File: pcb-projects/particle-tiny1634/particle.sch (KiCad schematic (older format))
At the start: 16 parts, among them IC1 ATTINY1634-SU, P1 CONN_02X03, P2 CONN_02X03

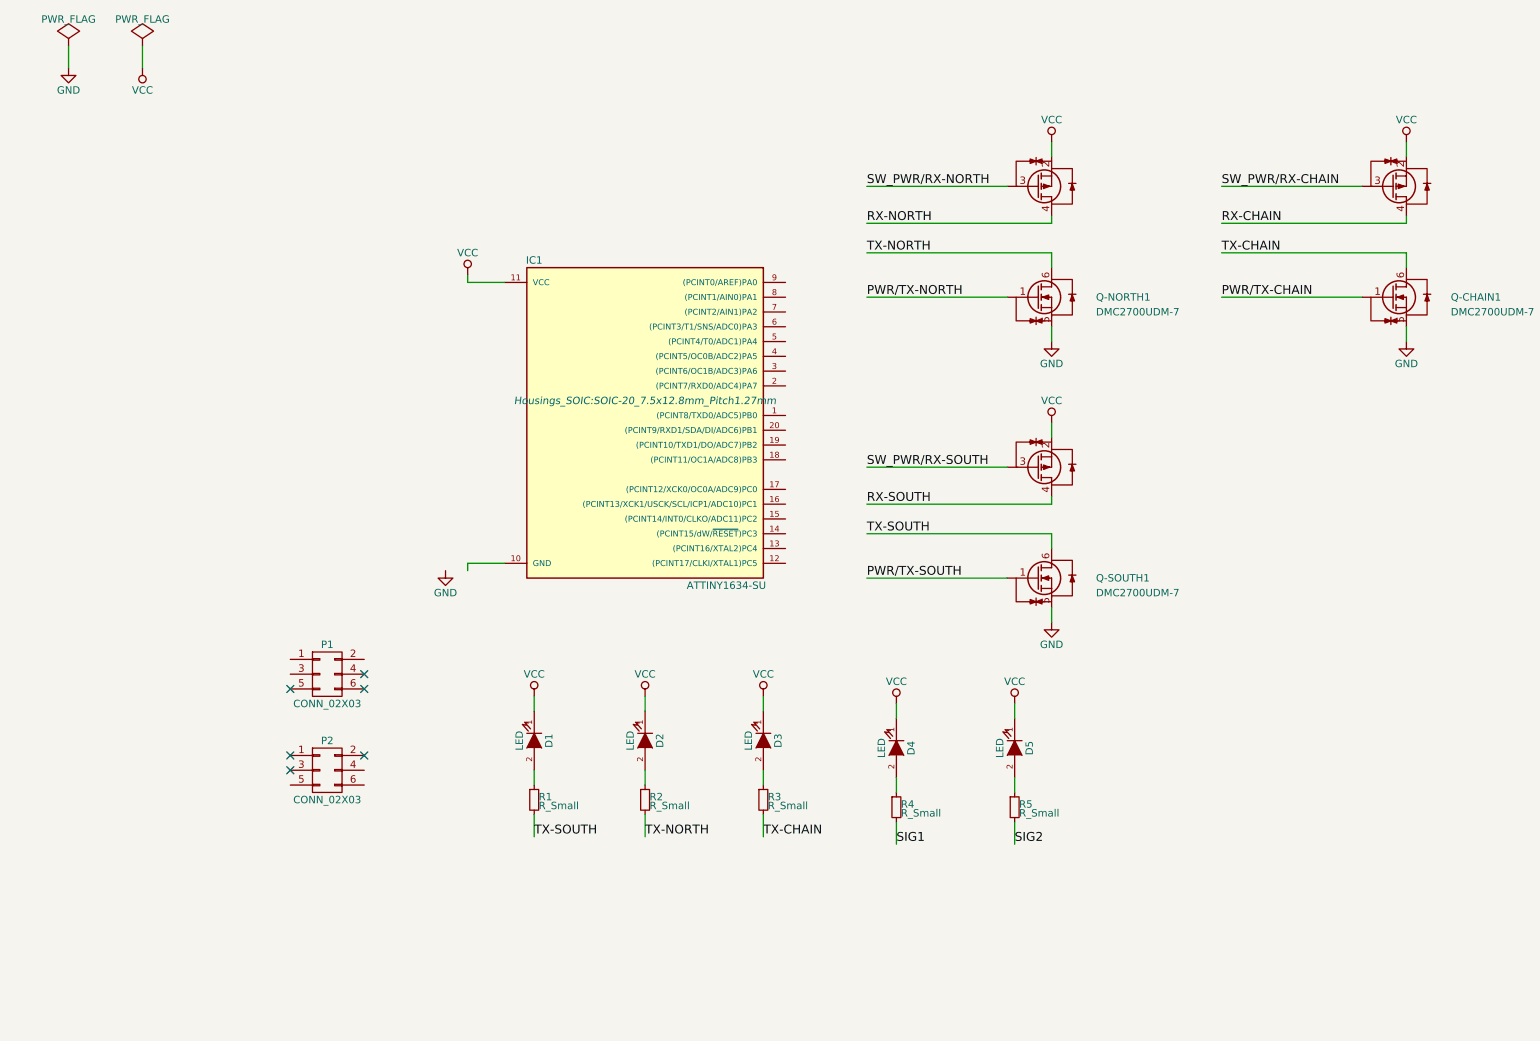
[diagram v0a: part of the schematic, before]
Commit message: routed attiny1634 particle
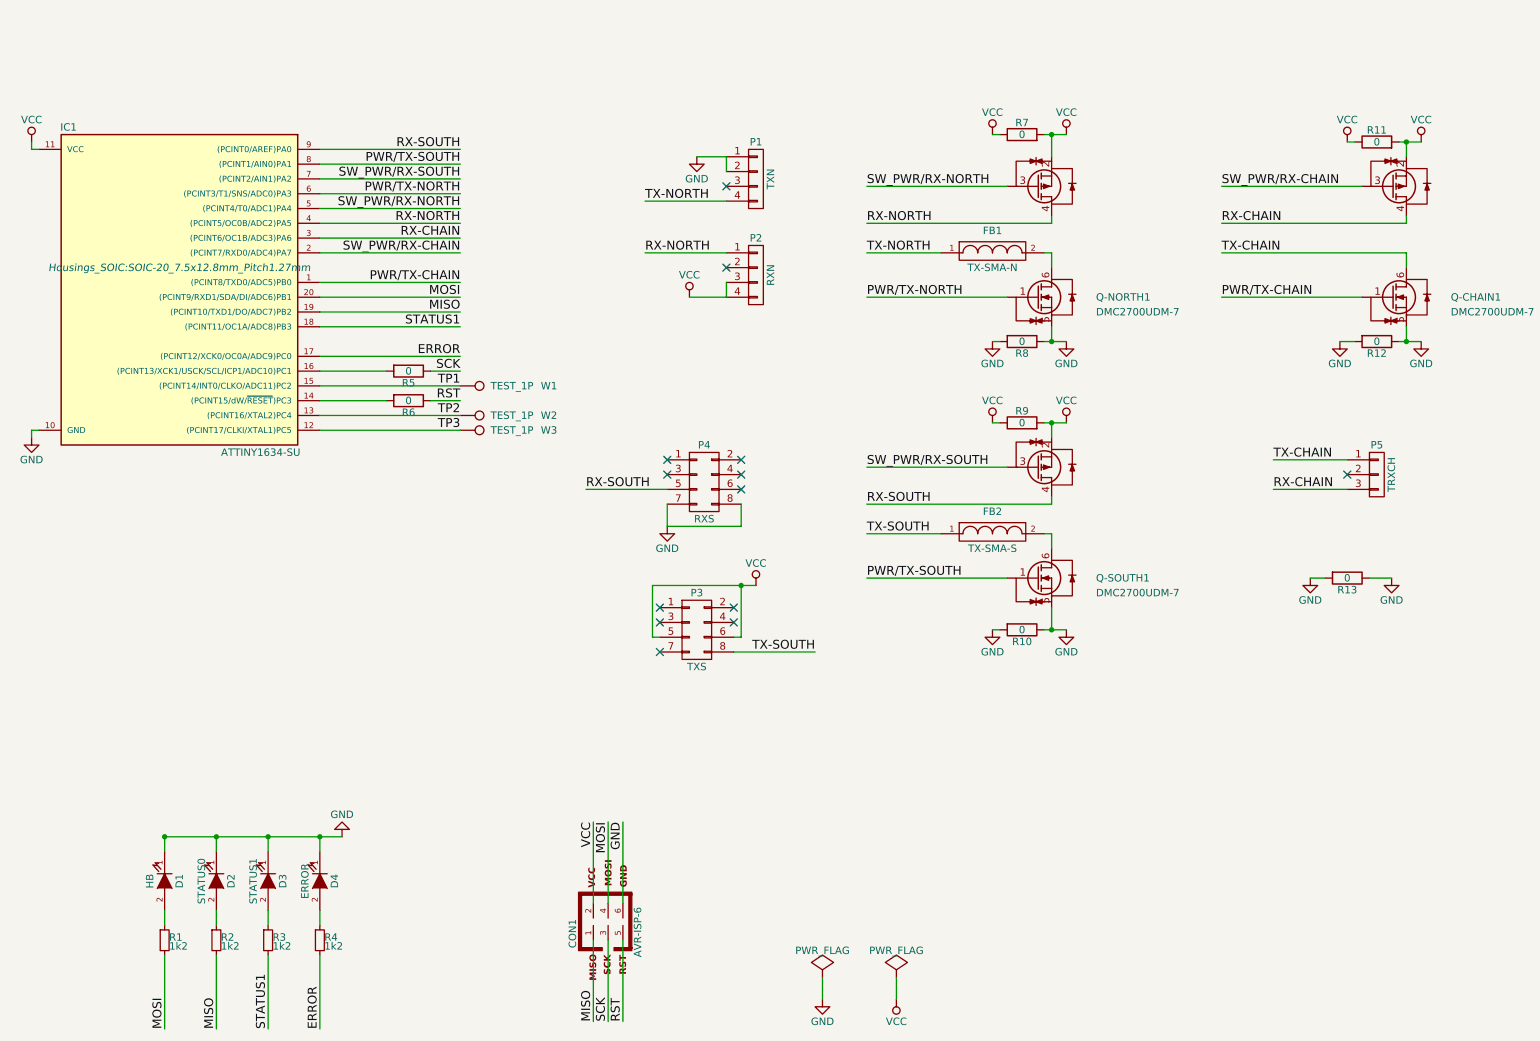
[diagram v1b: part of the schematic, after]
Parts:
- removed D1, D2: LED, LEDs:LED-1206, symbol LED
- removed P1: CONN_02X03, SMT_PIN_HEADER:CONN-6_1-3, symbol CONN_02X03
- removed P2: CONN_02X03, SMT_PIN_HEADER:CONN-6_4-6, symbol CONN_02X03
- removed R1, R2: R_Small, SMD_Packages:SMD-1206_Pol, symbol R_Small
- added CON1: AVR-ISP-6, SMT_PIN_HEADER:CONN-6, symbol AVR-ISP-6
- added D4: ERROR, Resistors_SMD:R_1206_HandSoldering, symbol LED
- added FB1: TX-SMA-N, SMD_Packages:SMD-2010_Pol, symbol FILTER
- added FB2: TX-SMA-S, SMD_Packages:SMD-2010_Pol, symbol FILTER
- added P1: TXN, SMT_PIN_HEADER:CONN-8_1-4, symbol CONN_01X04
- added P2: RXN, SMT_PIN_HEADER:CONN-8_1-4, symbol CONN_01X04
- added P3: TXS, SMT_PIN_HEADER:CONN-8_5-8, symbol CONN_02X04
- added P4: RXS, SMT_PIN_HEADER:CONN-8_5-8, symbol CONN_02X04
- added P5: TRXCH, SMT_PIN_HEADER:CONN-1x3, symbol CONN_01X03
- added R10, R11, R12, R13, R5, R6, R7, R8, R9: 0, Resistors_SMD:R_1206_HandSoldering, symbol R
- added R4: 1k2, Resistors_SMD:R_1206_HandSoldering, symbol R_Small
- added W1, W2, W3: TEST_1P, Measurement_Points:Measurement_Point_Square-SMD-Pad_Big, symbol TEST_1P
- D1: renamed from D4; value LED -> HB; footprint LEDs:LED-1206 -> Resistors_SMD:R_1206_HandSoldering
- D2: renamed from D5; value LED -> STATUS0; footprint LEDs:LED-1206 -> Resistors_SMD:R_1206_HandSoldering
- D3: value LED -> STATUS1; footprint LEDs:LED-1206 -> Resistors_SMD:R_1206_HandSoldering
- R1: renamed from R4; value R_Small -> 1k2; footprint SMD_Packages:SMD-1206_Pol -> Resistors_SMD:R_1206_HandSoldering
- R2: renamed from R5; value R_Small -> 1k2; footprint SMD_Packages:SMD-1206_Pol -> Resistors_SMD:R_1206_HandSoldering
- R3: value R_Small -> 1k2; footprint SMD_Packages:SMD-1206_Pol -> Resistors_SMD:R_1206_HandSoldering
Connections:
- net SIG1 is gone; now on net MOSI: R1.2
- net SIG2 is gone; now on net MISO: R2.2
- net GND: now also D1.1 (K), D2.1 (K), D3.1 (K), IC1.10 (GND), CON1.6, D4.1 (K), P1.1 (P1), P1.2 (P2), P4.7 (P7), P4.8 (P8), R10.1, R10.2, R12.1, R12.2, R13.1, R13.2, R8.1, R8.2
- net PWR/TX-CHAIN: now also IC1.1 ((PCINT8/TXD0/ADC5)PB0)
- net PWR/TX-NORTH: now also IC1.6 ((PCINT3/T1/SNS/ADC0)PA3)
- net PWR/TX-SOUTH: now also IC1.8 ((PCINT1/AIN0)PA1)
- net RX-CHAIN: now also IC1.3 ((PCINT6/OC1B/ADC3)PA6), P5.3 (P3)
- net RX-NORTH: now also IC1.4 ((PCINT5/OC0B/ADC2)PA5), P2.1 (P1)
- net RX-SOUTH: now also IC1.9 ((PCINT0/AREF)PA0), P4.5 (P5)
- net SW_PWR/RX-CHAIN: now also IC1.2 ((PCINT7/RXD0/ADC4)PA7)
- net SW_PWR/RX-NORTH: now also IC1.5 ((PCINT4/T0/ADC1)PA4)
- net SW_PWR/RX-SOUTH: now also IC1.7 ((PCINT2/AIN1)PA2)
- net TX-CHAIN: now also P5.1 (P1); no longer R3.2
- net TX-NORTH: now also FB1.1, P1.4 (P4); no longer Q-NORTH1.6 (D1)
- net TX-SOUTH: now also FB2.1, P3.8 (P8); no longer Q-SOUTH1.6 (D1)
- net VCC: now also CON1.2, P2.3 (P3), P2.4 (P4), P3.5 (P5), P3.6 (P6), R11.1, R11.2, R7.1, R7.2, R9.1, R9.2; no longer D1.1 (K), D2.1 (K), D3.1 (K)
- net TP3: now reaches IC1.12 ((PCINT17/CLKI/XTAL1)PC5)
- net TP3: now also W3.1
- net TP2: now reaches IC1.13 ((PCINT16/XTAL2)PC4)
- net TP2: now also W2.1
- net at IC1.14 ((PCINT15/dW/~RESET~)PC3): now also R6.2
- net TP1: now reaches IC1.15 ((PCINT14/INT0/CLKO/ADC11)PC2)
- net TP1: now also W1.1
- net at IC1.16 ((PCINT13/XCK1/USCK/SCL/ICP1/ADC10)PC1): now also R5.2
- net ERROR: now reaches IC1.17 ((PCINT12/XCK0/OC0A/ADC9)PC0)
- net ERROR: now also R4.2
- net STATUS1: now reaches IC1.18 ((PCINT11/OC1A/ADC8)PB3)
- net STATUS1: now also R3.2
- net MISO: now reaches IC1.19 ((PCINT10/TXD1/DO/ADC7)PB2)
- net MISO: now also CON1.1
- net MOSI: now reaches IC1.20 ((PCINT9/RXD1/SDA/DI/ADC6)PB1)
- net MOSI: now also CON1.4
- new net: FB1.2, Q-NORTH1.6 (D1)
- new net: FB2.2, Q-SOUTH1.6 (D1)
- new net: D4.2 (A), R4.1
- new net RST: CON1.5, R6.1
- new net SCK: CON1.3, R5.1
- no-connect marks 6 -> 13
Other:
- moved on the sheet: D1, D2, IC1, R1, R2

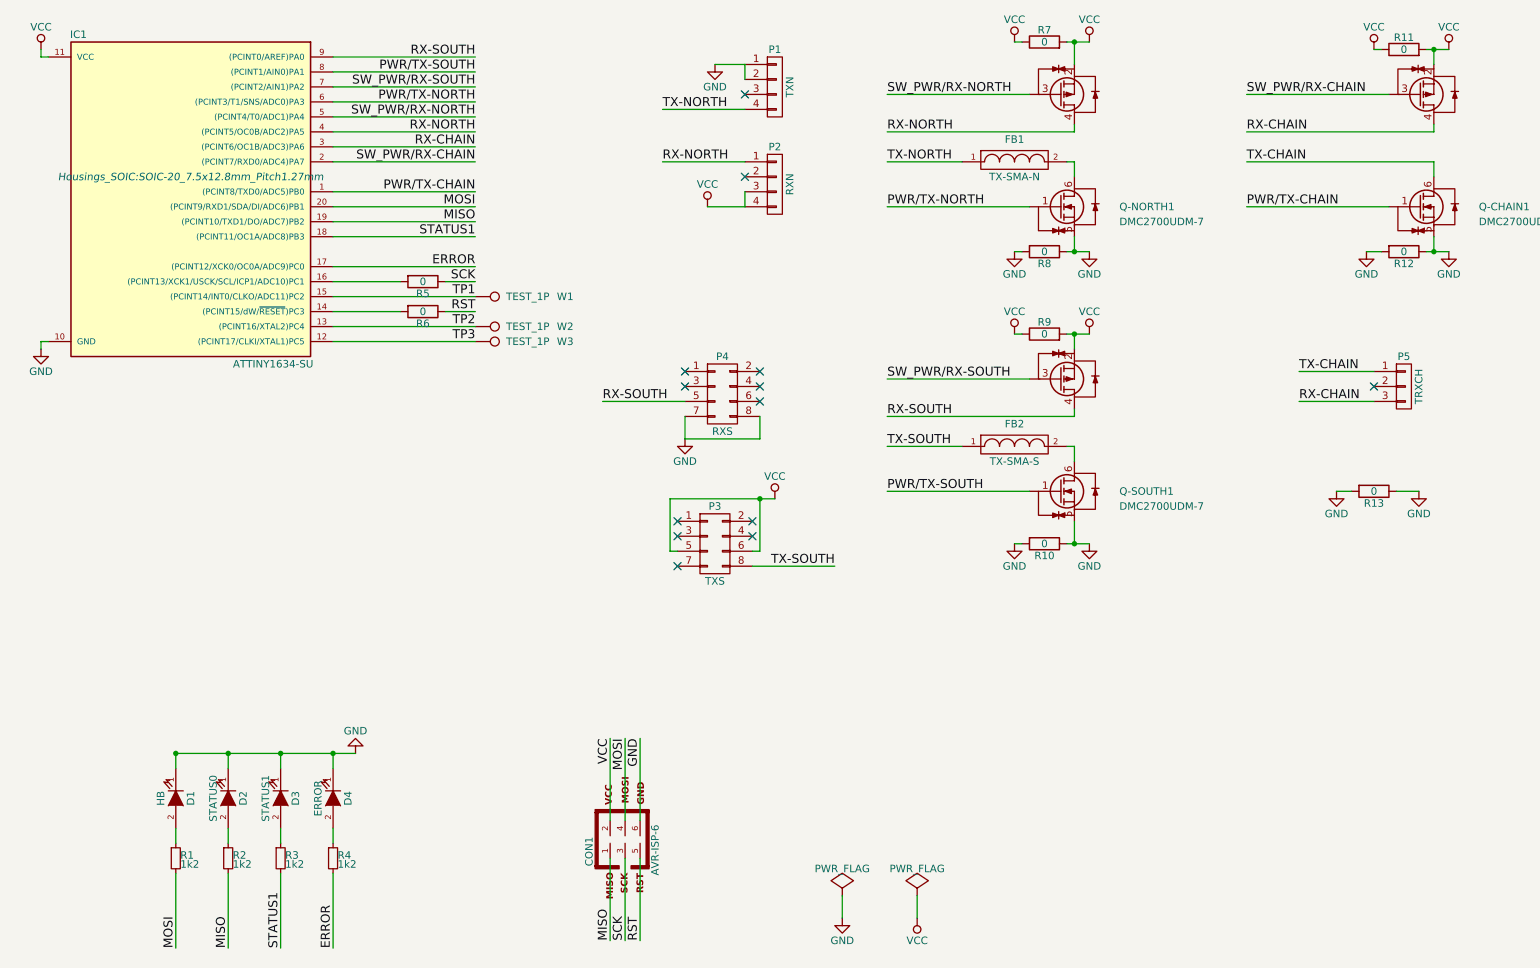
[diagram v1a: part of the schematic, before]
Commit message: re-routed smaller pcb, added several 3d packages, min. fix in schema
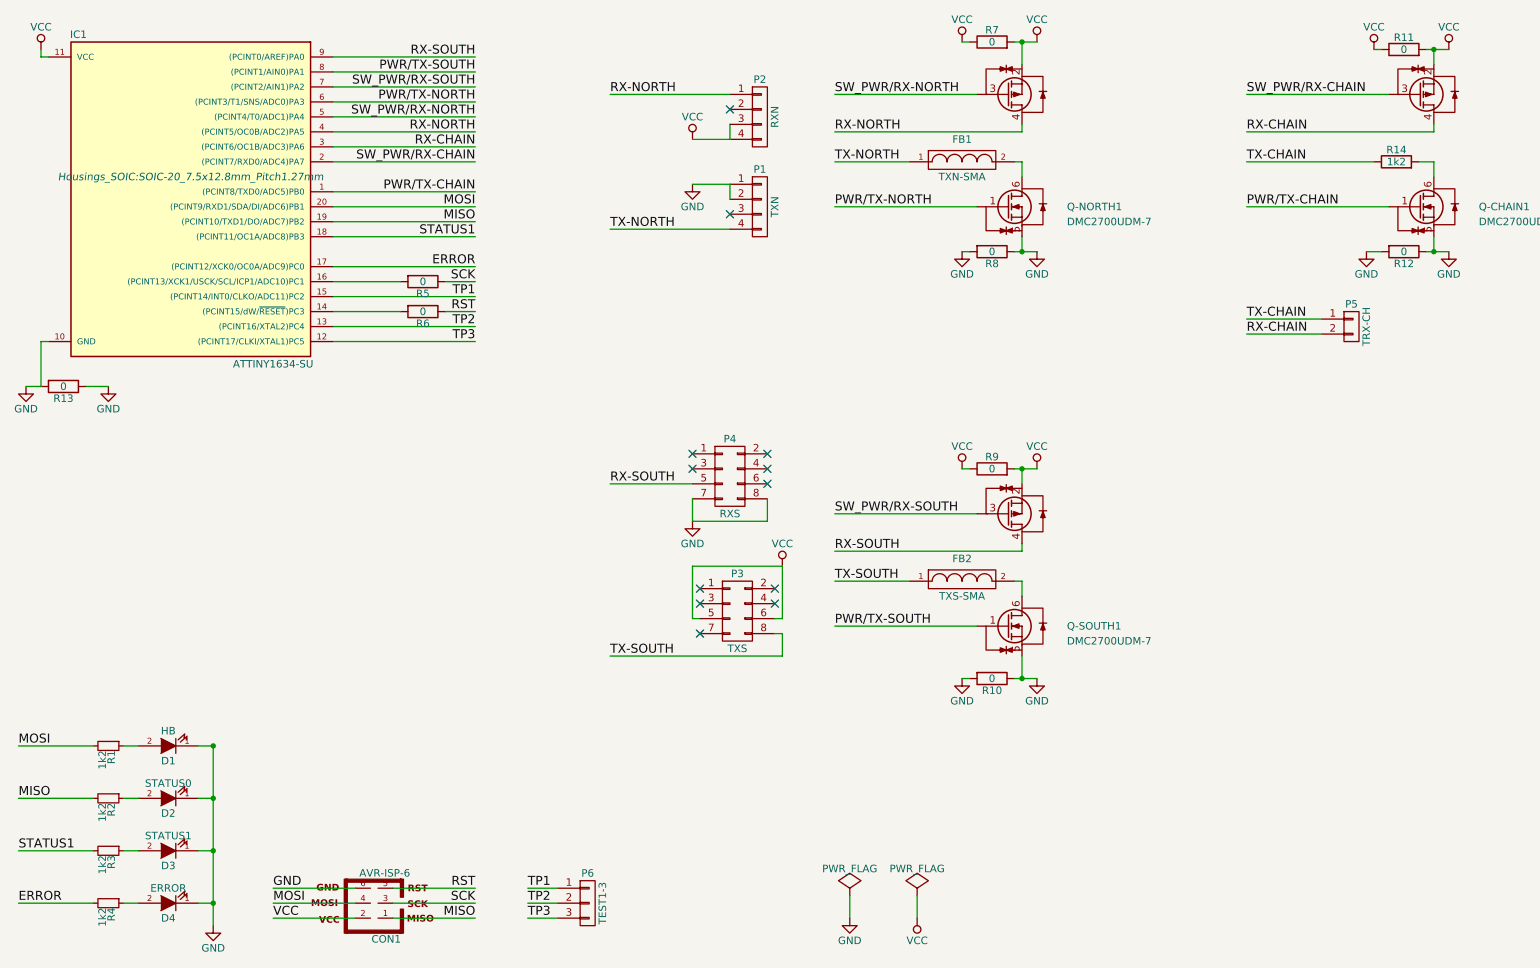
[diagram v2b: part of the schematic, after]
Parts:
- removed P5: TRXCH, SMT_PIN_HEADER:CONN-1x3, symbol CONN_01X03
- removed W1, W2, W3: TEST_1P, Measurement_Points:Measurement_Point_Square-SMD-Pad_Big, symbol TEST_1P
- added P5: TRX-CH, SMT_PIN_HEADER:CONN-1x2, symbol CONN_01X02
- added P6: TEST1-3, SMT_PIN_HEADER:CONN-1x3, symbol CONN_01X03
- added R14: 1k2, Resistors_SMD:R_1206_HandSoldering, symbol R
- FB1: value TX-SMA-N -> TXN-SMA
- FB2: value TX-SMA-S -> TXS-SMA
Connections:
- net RX-CHAIN: now also P5.2 (P2)
- net TP1: now also P6.1 (P1)
- net TP2: now also P6.2 (P2)
- net TP3: now also P6.3 (P3)
- net TX-CHAIN: now also P5.1 (P1), R14.1; no longer Q-CHAIN1.6 (D1)
- new net: Q-CHAIN1.6 (D1), R14.2
- no-connect marks 13 -> 12
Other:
- moved on the sheet: CON1, D1, D2, D3, D4, FB1, FB2, P1, P2, P3, P4, Q-NORTH1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
